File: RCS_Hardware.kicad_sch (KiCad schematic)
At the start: 48 parts, among them J1 SWD, J2 TYPE-C-31-M-12, J3 JST BATT, J4 3V3, J5 GND, U1 STM32F401CCU6, U2 AMS1117-3.3, U3 BMP280, U4 BNO055, U5 W25Q32JVSS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

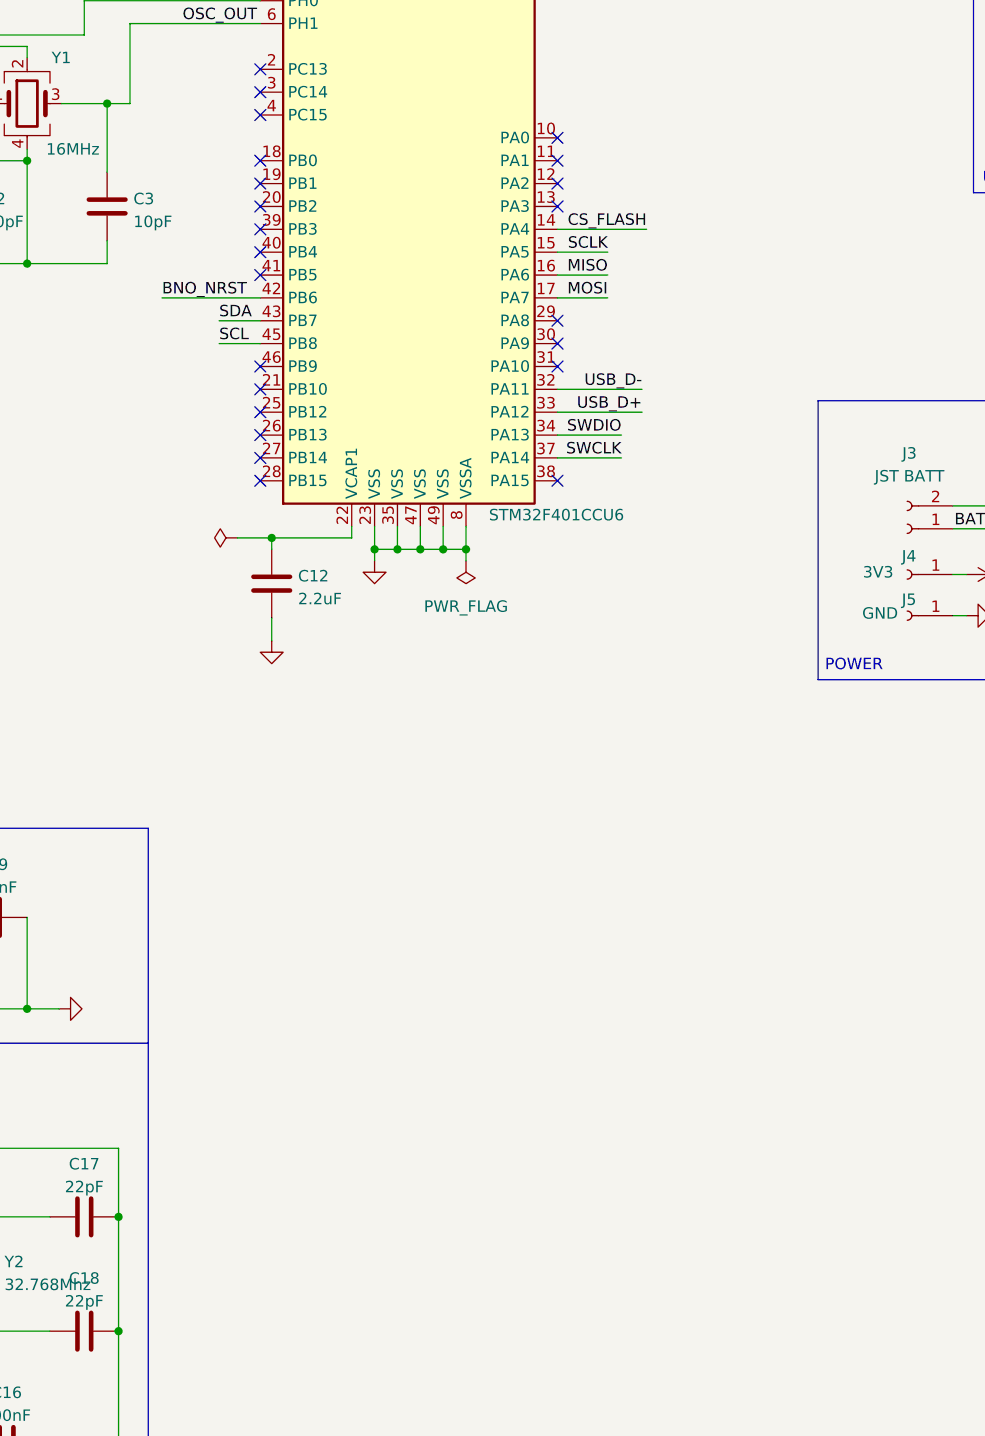
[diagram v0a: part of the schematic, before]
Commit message: added solenoid control pins added external sensor pins added green and blue status leds updated render
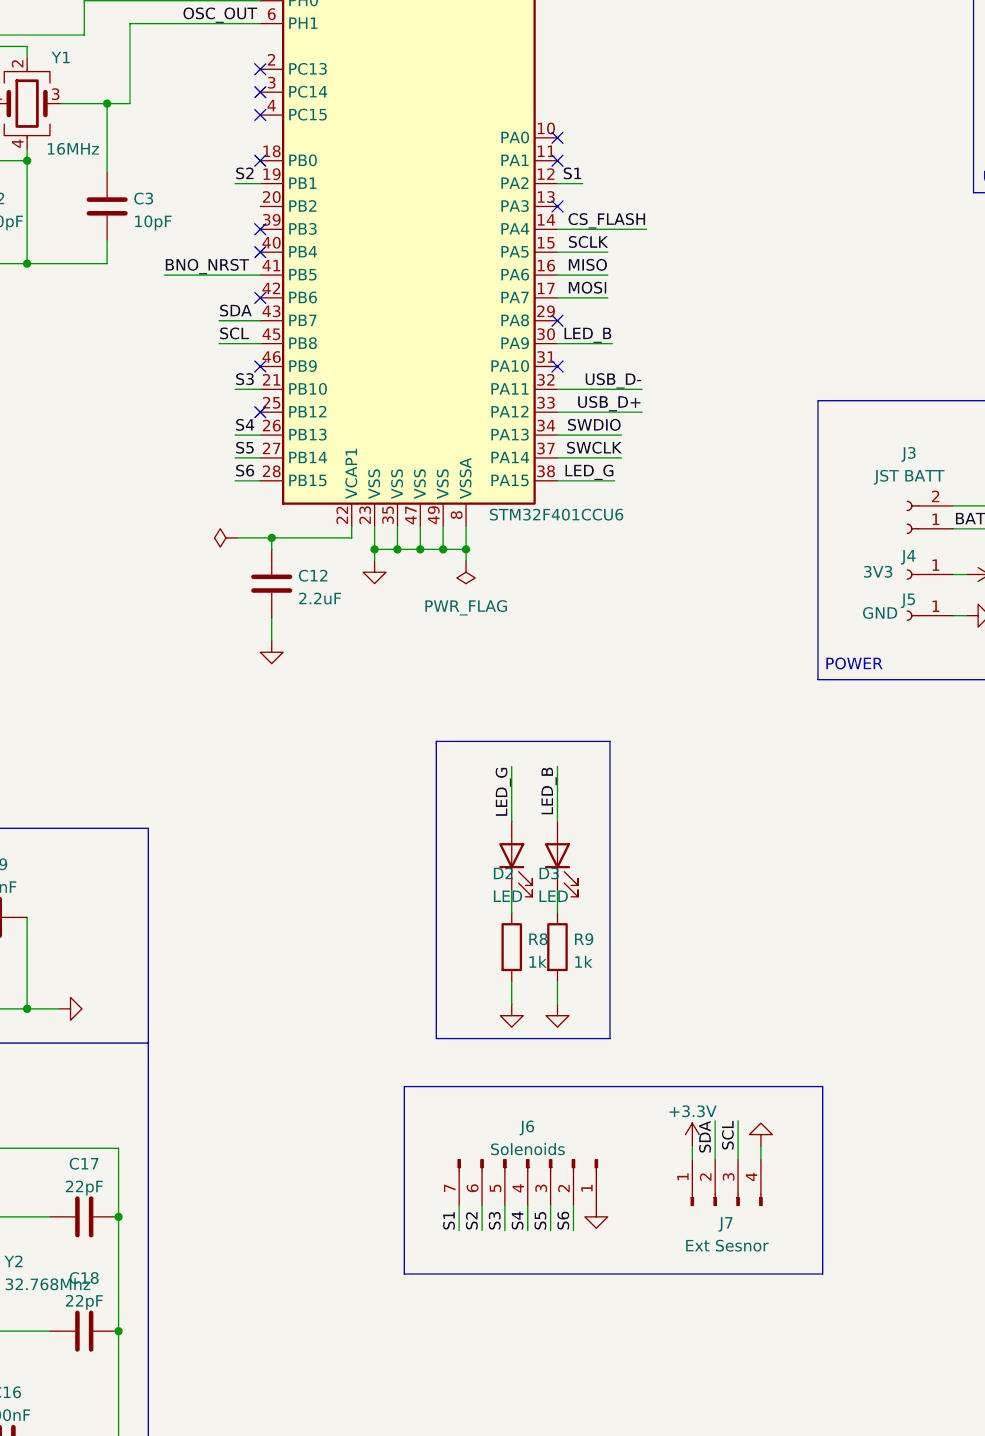
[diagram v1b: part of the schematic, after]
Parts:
- added D2, D3: LED, LED_SMD:LED_0603_1608Metric, symbol Device:LED
- added J6: Solenoids, Connector_PinHeader_2.54mm:PinHeader_1x07_P2.54mm_Vertical, symbol Connector:Conn_01x07_Male
- added J7: Ext Sesnor, Connector_PinHeader_2.54mm:PinHeader_1x04_P2.54mm_Vertical, symbol Connector:Conn_01x04_Male
- added R8, R9: 1k, Resistor_SMD:R_0402_1005Metric, symbol Device:R
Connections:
- net +3.3V: now also J7.1 (Pin_1)
- net BNO_NRST: now also U1.41 (PB5); no longer U1.42 (PB6)
- net GND: now also J6.1 (Pin_1), J7.4 (Pin_4), R8.2, R9.2
- net SCL: now also J7.3 (Pin_3)
- net SDA: now also J7.2 (Pin_2)
- net S1: now reaches U1.12 (PA2)
- net S1: now also J6.7 (Pin_7)
- net S2: now reaches U1.19 (PB1)
- net S2: now also J6.6 (Pin_6)
- net S3: now reaches U1.21 (PB10)
- net S3: now also J6.5 (Pin_5)
- net S4: now reaches U1.26 (PB13)
- net S4: now also J6.4 (Pin_4)
- net S5: now reaches U1.27 (PB14)
- net S5: now also J6.3 (Pin_3)
- net S6: now reaches U1.28 (PB15)
- net S6: now also J6.2 (Pin_2)
- net LED_B: now reaches U1.30 (PA9)
- net LED_B: now also D3.2 (A)
- net LED_G: now reaches U1.38 (PA15)
- net LED_G: now also D2.2 (A)
- new net: D2.1 (K), R8.1
- new net: D3.1 (K), R9.1
- no-connect marks 32 -> 23

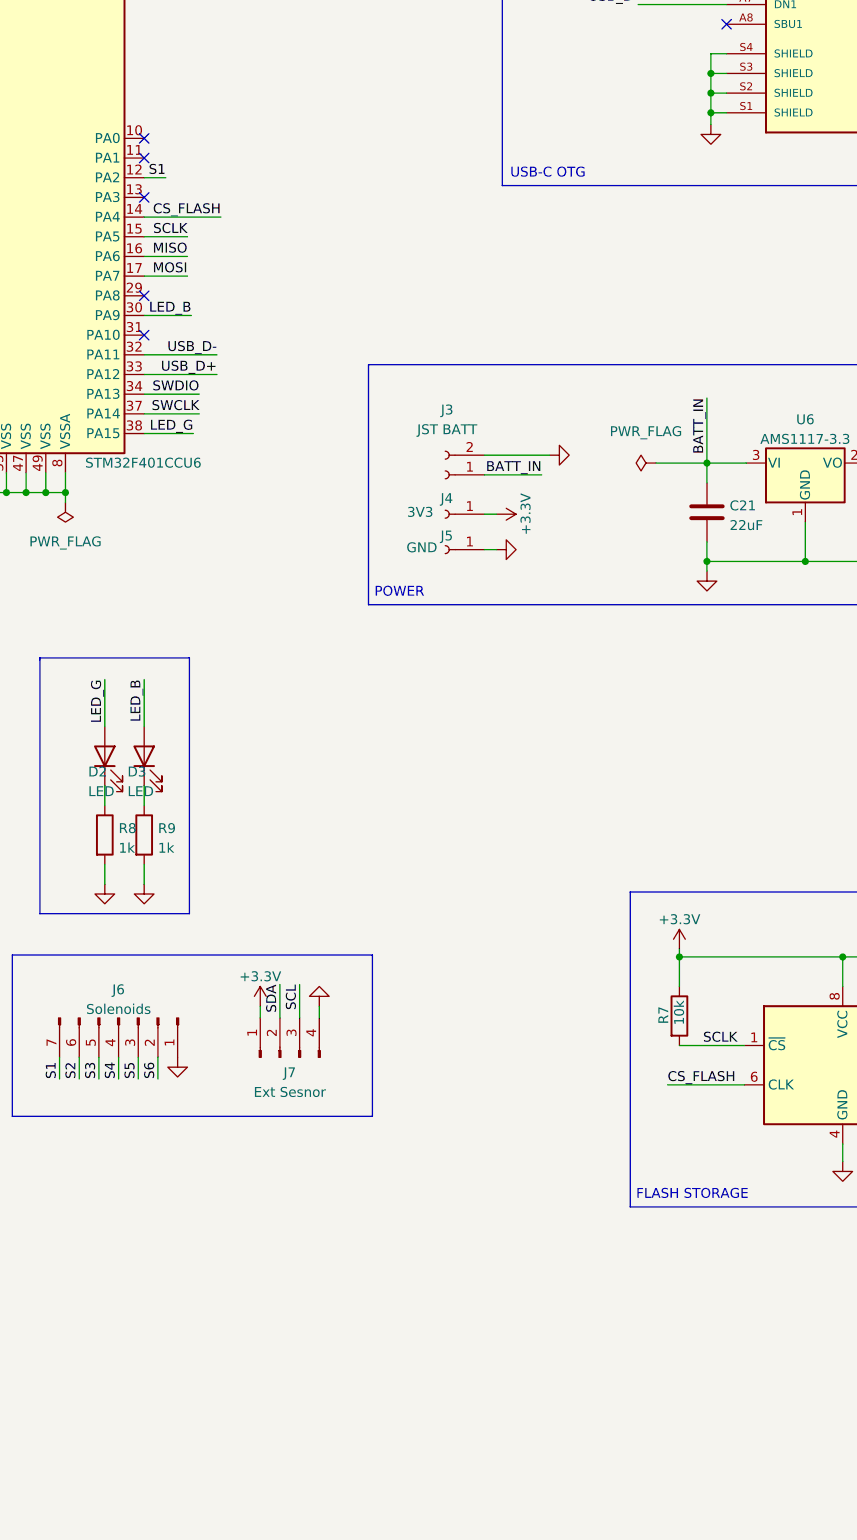
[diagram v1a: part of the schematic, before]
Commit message: created symbol and footprint for differential driver added schema for diff driver layed out diff driver and connector updated render
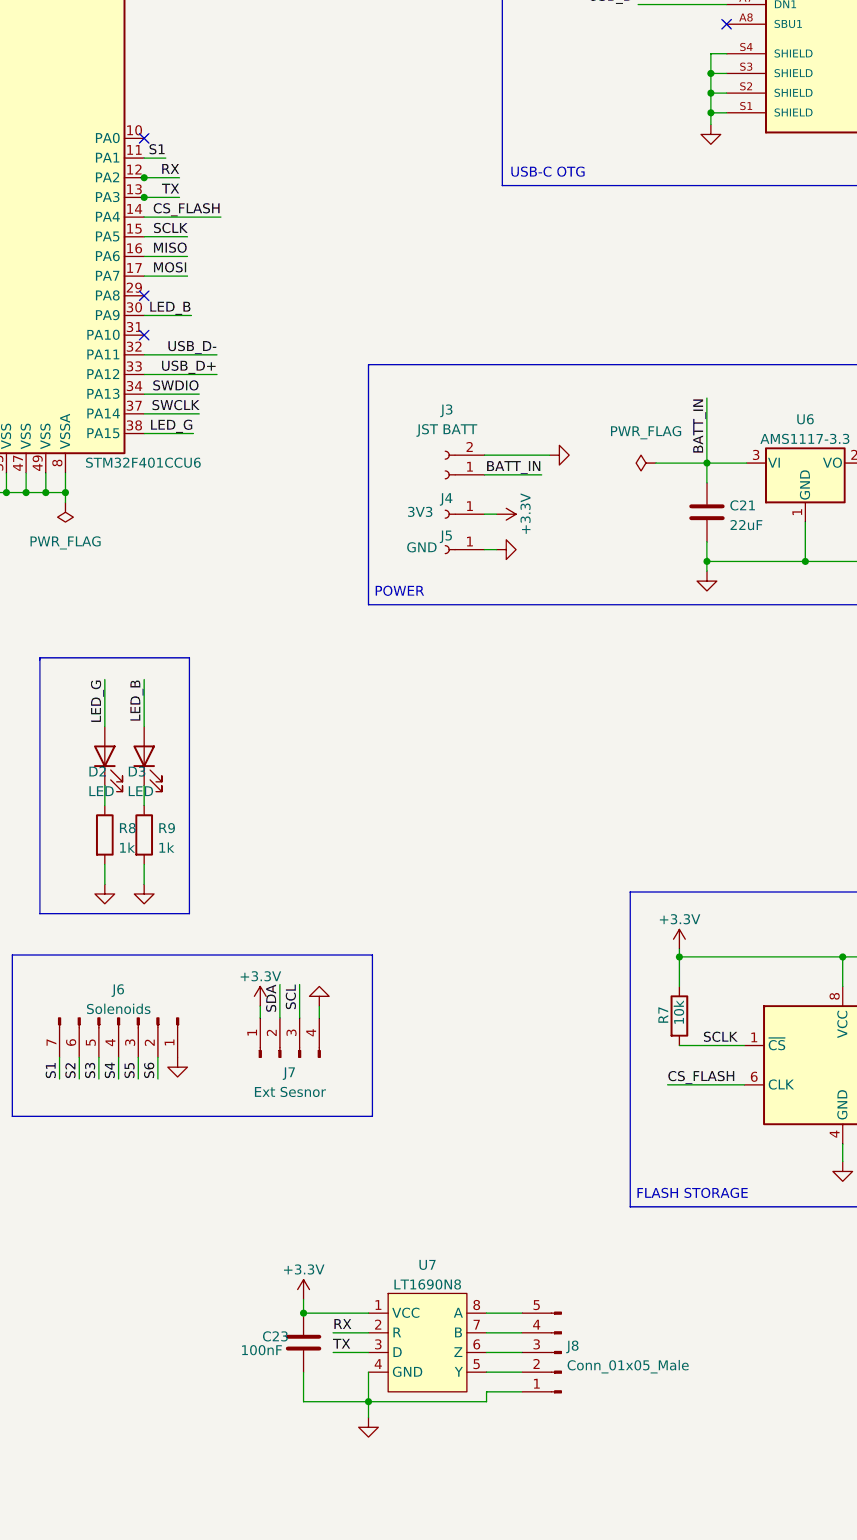
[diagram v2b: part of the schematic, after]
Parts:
- added C23: 100nF, Capacitor_SMD:C_0402_1005Metric, symbol Device:C
- added J8: Conn_01x05_Male, Connector_PinHeader_2.54mm:PinHeader_1x05_P2.54mm_Vertical, symbol Connector:Conn_01x05_Male
- added U7: LT1690N8, LTC1690N8:LTC1690N8, symbol lt1690n8:LT1690N8
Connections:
- net +3.3V: now also C23.1, U7.1 (VCC)
- net GND: now also C23.2, J8.1 (Pin_1), U7.4 (GND)
- net S1: now also U1.11 (PA1); no longer U1.12 (PA2)
- net TX: now reaches U1.13 (PA3)
- net TX: now also U7.3 (D)
- new net: J8.2 (Pin_2), U7.5 (Y)
- new net: J8.3 (Pin_3), U7.6 (Z)
- new net: J8.4 (Pin_4), U7.7 (B)
- new net: J8.5 (Pin_5), U7.8 (A)
- new net RX: U1.12 (PA2), U7.2 (R)
- no-connect marks 23 -> 21
